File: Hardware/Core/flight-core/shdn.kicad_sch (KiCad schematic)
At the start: 24 parts, among them J15 Conn_02x02_Remote_ESTOP, J16 Conn_02x07_Counter_Clockwise, J17 TILT, J18 Conn_02x02_Remote_ESTOP, J19 Conn_01x02, J20 Conn_02x02_Remote_ESTOP, J21 Conn_02x02_Remote_ESTOP, J22 Conn_02x02_Remote_ESTOP, J23 Conn_02x02_Remote_ESTOP, J24 Conn_02x02_Remote_ESTOP, J25 Conn_02x02_Remote_ESTOP, J26 Conn_02x02_Remote_ESTOP, J27 Conn_02x02_Remote_ESTOP, Q4 MMBF170, U50 LTV-356T, U51 LTV-356T

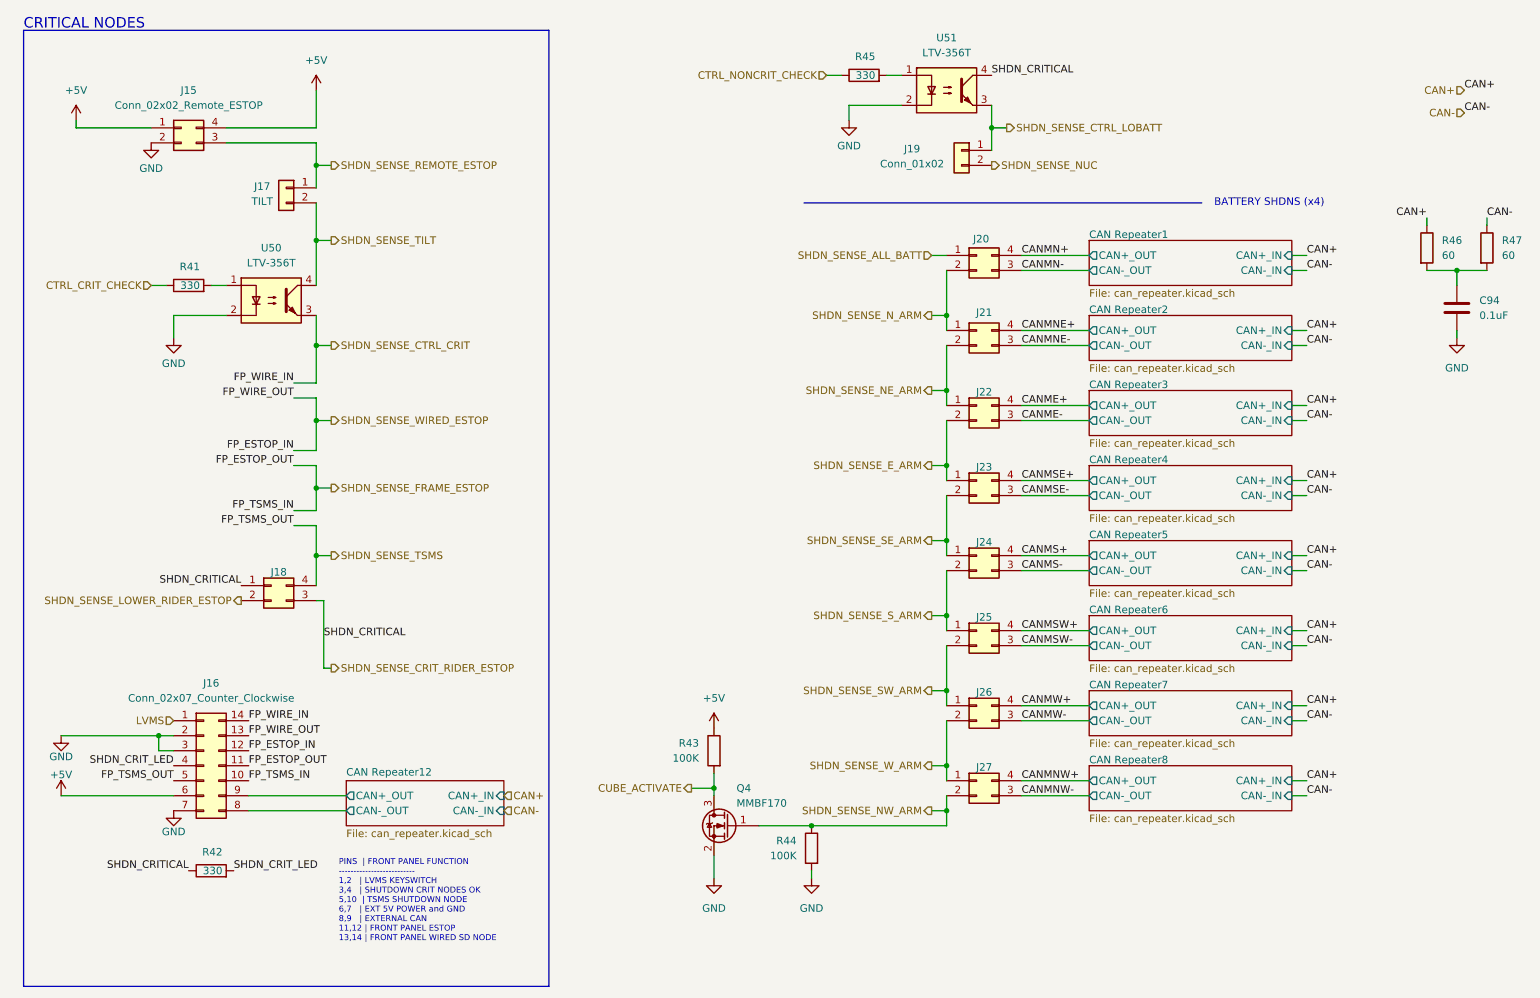
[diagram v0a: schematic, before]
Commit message: major component area placement begun, installing place footprints plugin, updating connectors to vertical
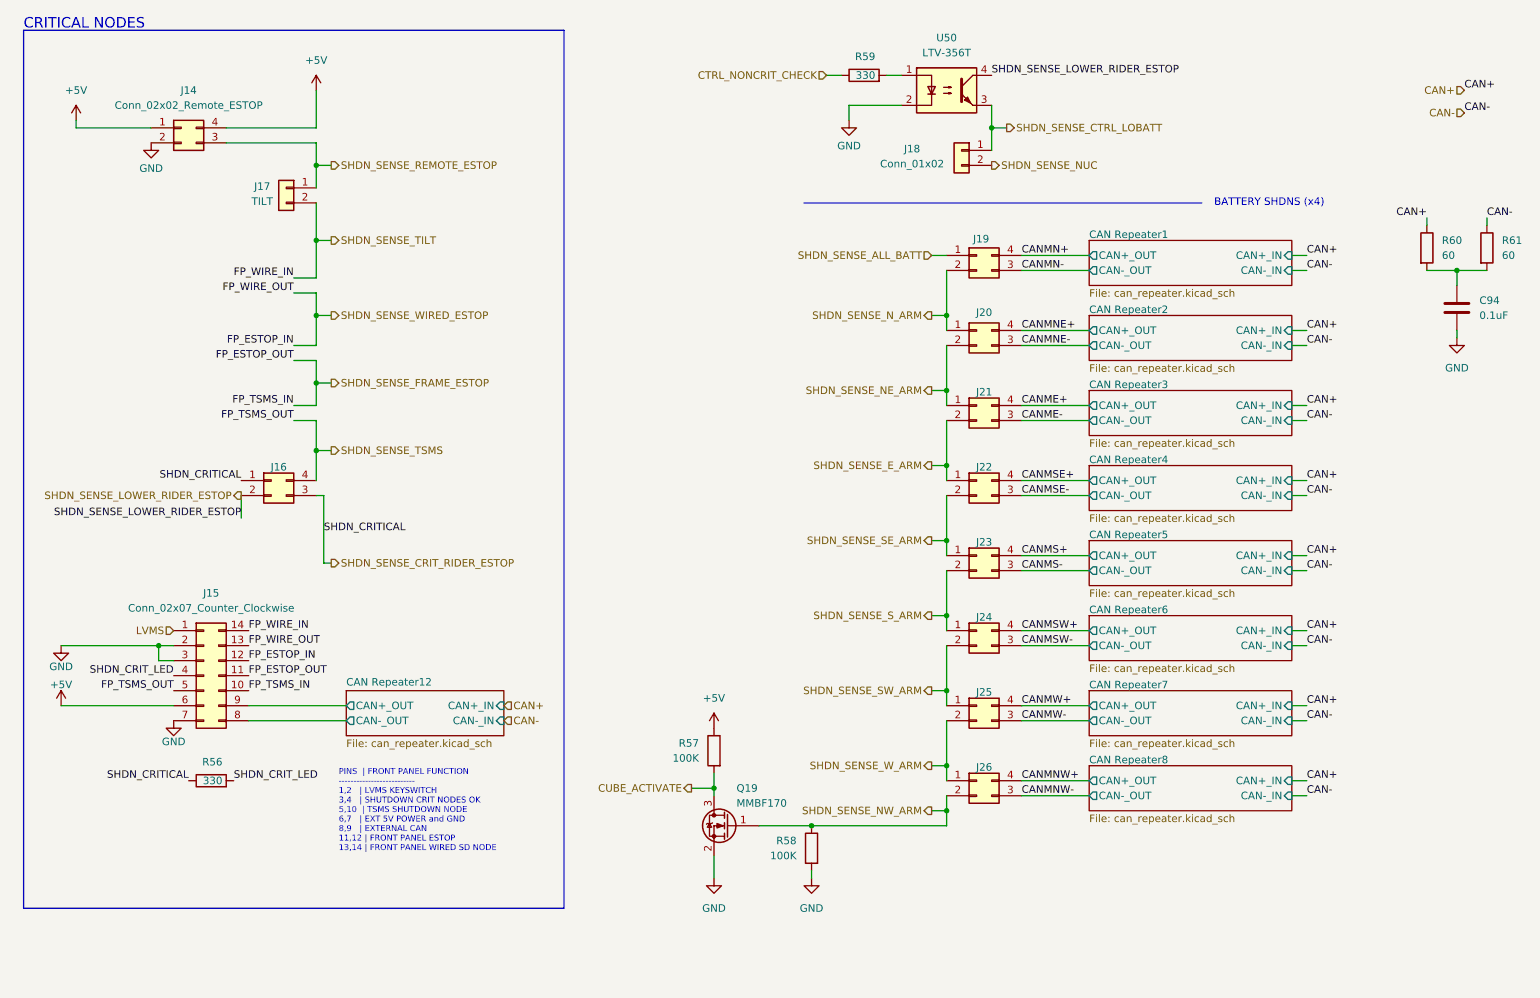
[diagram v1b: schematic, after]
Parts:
- removed R41: 330, footprints:R_0603_1608Metric, symbol Device:R
- removed U50: LTV-356T, Package_SO:SO-4_4.4x3.6mm_P2.54mm, symbol Isolator:LTV-356T
- renumbered J15 to J14, J16 to J15, J18 to J16, J19 to J18, J20 to J19, J21 to J20, J22 to J21, J23 to J22, J24 to J23, J25 to J24, J26 to J25, J27 to J26, Q4 to Q19, R42 to R56, R43 to R57, R44 to R58, R45 to R59, R46 to R60, R47 to R61, U51 to U50
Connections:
- net SHDN_SENSE_CTRL_CRIT is gone; now on net SHDN_SENSE_TILT: J15.14 (Pin_14)
- net SHDN_SENSE_CRIT_RIDER_ESTOP: no longer U50.4
- net SHDN_SENSE_LOWER_RIDER_ESTOP: now also U50.4
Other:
- moved on the sheet: J15, J16, R56

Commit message: can repeater placement, custom cube footprint, connector placement
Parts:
- J14, J16, J19, J20, J21, J22, J23, J24, J25, J26: footprint Connector_Molex:Molex_Micro-Fit_3.0_43045-0400_2x02_P3.00mm_Horizontal -> Connector_Molex:Molex_Micro-Fit_3.0_43045-0412_2x02_P3.00mm_Vertical
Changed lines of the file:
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@@
 			)
 		)
-		(property "Footprint" "Connector_Molex:Molex_Micro-Fit_3.0_43045-0400_2x02_P3.00mm_Horizontal"
+		(property "Footprint" "Connector_Molex:Molex_Micro-Fit_3.0_43045-0412_2x02_P3.00mm_Vertical"
 			(at 182.88 151.13 0)
 			(effects
@@
 			)
 		)
-		(property "Footprint" "Connector_Molex:Molex_Micro-Fit_3.0_43045-0400_2x02_P3.00mm_Horizontal"
+		(property "Footprint" "Connector_Molex:Molex_Micro-Fit_3.0_43045-0412_2x02_P3.00mm_Vertical"
 			(at 182.88 87.63 0)
 			(effects
@@
 			)
 		)
-		(property "Footprint" "Connector_Molex:Molex_Micro-Fit_3.0_43045-0400_2x02_P3.00mm_Horizontal"
+		(property "Footprint" "Connector_Molex:Molex_Micro-Fit_3.0_43045-0412_2x02_P3.00mm_Vertical"
 			(at 182.88 74.93 0)
 			(effects
@@
 			)
 		)
-		(property "Footprint" "Connector_Molex:Molex_Micro-Fit_3.0_43045-0400_2x02_P3.00mm_Horizontal"
+		(property "Footprint" "Connector_Molex:Molex_Micro-Fit_3.0_43045-0412_2x02_P3.00mm_Vertical"
 			(at 182.88 138.43 0)
 			(effects
@@
 			)
 		)
-		(property "Footprint" "Connector_Molex:Molex_Micro-Fit_3.0_43045-0400_2x02_P3.00mm_Horizontal"
+		(property "Footprint" "Connector_Molex:Molex_Micro-Fit_3.0_43045-0412_2x02_P3.00mm_Vertical"
 			(at 63.5 100.33 0)
 			(effects
@@
 			)
 		)
-		(property "Footprint" "Connector_Molex:Molex_Micro-Fit_3.0_43045-0400_2x02_P3.00mm_Horizontal"
+		(property "Footprint" "Connector_Molex:Molex_Micro-Fit_3.0_43045-0412_2x02_P3.00mm_Vertical"
 			(at 182.88 113.03 0)
 			(effects
@@
 			)
 		)
-		(property "Footprint" "Connector_Molex:Molex_Micro-Fit_3.0_43045-0400_2x02_P3.00mm_Horizontal"
+		(property "Footprint" "Connector_Molex:Molex_Micro-Fit_3.0_43045-0412_2x02_P3.00mm_Vertical"
 			(at 182.88 62.23 0)
 			(effects
@@
 			)
 		)
-		(property "Footprint" "Connector_Molex:Molex_Micro-Fit_3.0_43045-0400_2x02_P3.00mm_Horizontal"
+		(property "Footprint" "Connector_Molex:Molex_Micro-Fit_3.0_43045-0412_2x02_P3.00mm_Vertical"
 			(at 182.88 125.73 0)
 			(effects
@@
 			)
 		)
-		(property "Footprint" "Connector_Molex:Molex_Micro-Fit_3.0_43045-0400_2x02_P3.00mm_Horizontal"
+		(property "Footprint" "Connector_Molex:Molex_Micro-Fit_3.0_43045-0412_2x02_P3.00mm_Vertical"
 			(at 182.88 100.33 0)
 			(effects
@@
 			)
 		)
-		(property "Footprint" "Connector_Molex:Molex_Micro-Fit_3.0_43045-0400_2x02_P3.00mm_Horizontal"
+		(property "Footprint" "Connector_Molex:Molex_Micro-Fit_3.0_43045-0412_2x02_P3.00mm_Vertical"
 			(at 48.26 40.64 0)
 			(effects

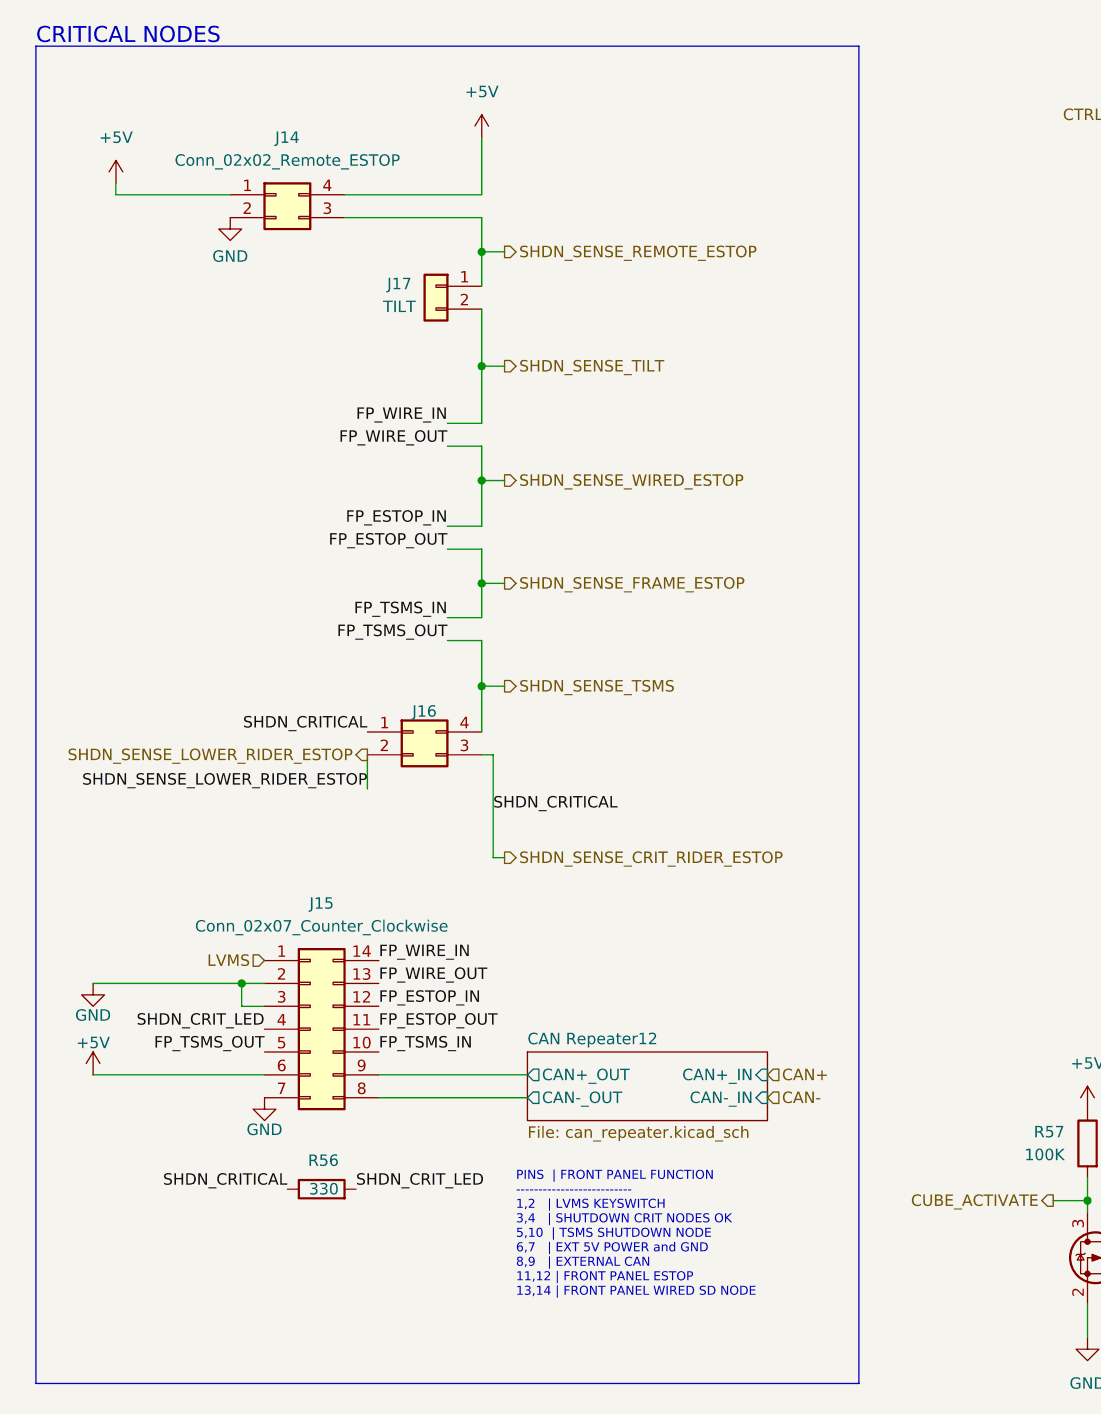
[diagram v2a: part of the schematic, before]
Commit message: corrected shdn fp connector, more led and can repeater placement
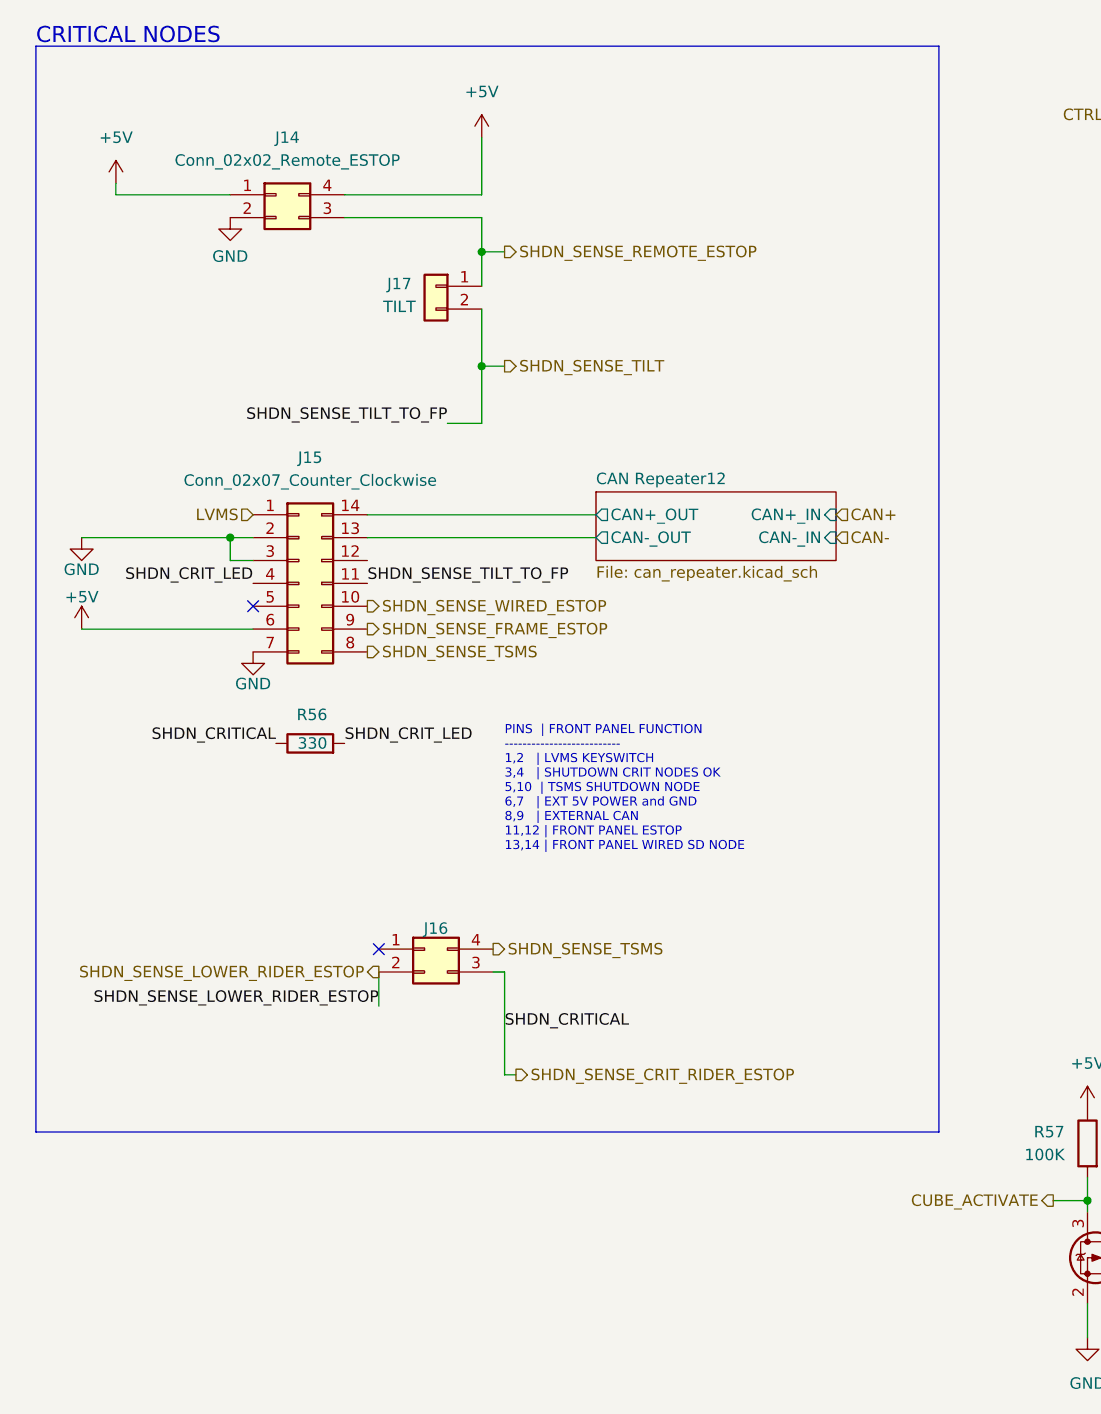
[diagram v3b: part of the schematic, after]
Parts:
- R57, R58: footprint footprints:R_0805_OEM -> footprints:R_0603_1608Metric
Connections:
- net CAN Repeater12/CAN+_OUT: now also J15.14 (Pin_14); no longer J15.9 (Pin_9)
- net CAN Repeater12/CAN-_OUT: now also J15.13 (Pin_13); no longer J15.8 (Pin_8)
- net SHDN_SENSE_CRIT_RIDER_ESTOP: no longer J16.1 (Pin_1)
- net SHDN_SENSE_FRAME_ESTOP: now also J15.9 (Pin_9); no longer J15.10 (Pin_10), J15.11 (Pin_11)
- net SHDN_SENSE_TILT: now also J15.11 (Pin_11); no longer J15.14 (Pin_14)
- net SHDN_SENSE_TSMS: now also J15.8 (Pin_8); no longer J15.5 (Pin_5)
- net SHDN_SENSE_WIRED_ESTOP: now also J15.10 (Pin_10); no longer J15.12 (Pin_12), J15.13 (Pin_13)
- no-connect marks 0 -> 2
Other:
- moved on the sheet: J15, J16, R56
